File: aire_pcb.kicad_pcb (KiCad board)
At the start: 2 copper layers, 79 x 54.2 mm, 52 parts, among them J1 Conn_01x02_Male, J2 Screw_Terminal_01x02, J3 Screw_Terminal_01x03, J4 Conn_01x04_Male, K1 JRC-21F_4100, K2 JRC-21F_4100, K3 JRC-21F_4100, Q1 2N3904, Q2 2N3904, Q3 2N3904, SW1 SW_Push, SW2 SW_Push, U1 NCP1117-3.3_SOT223, U2 HLK-2M05, U3 SHT40, U4 ESP8266-12E/ESP-12E

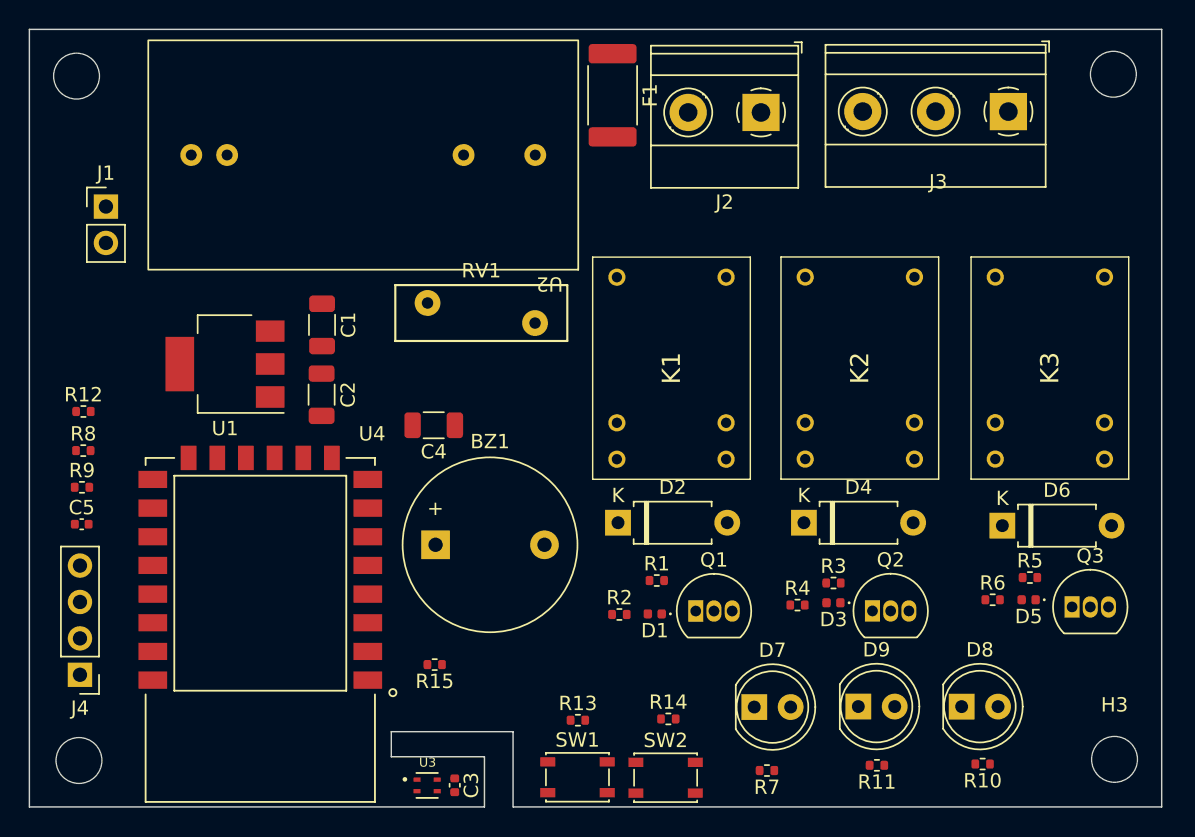
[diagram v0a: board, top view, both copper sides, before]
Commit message: Improve placement and add expansion conenctor
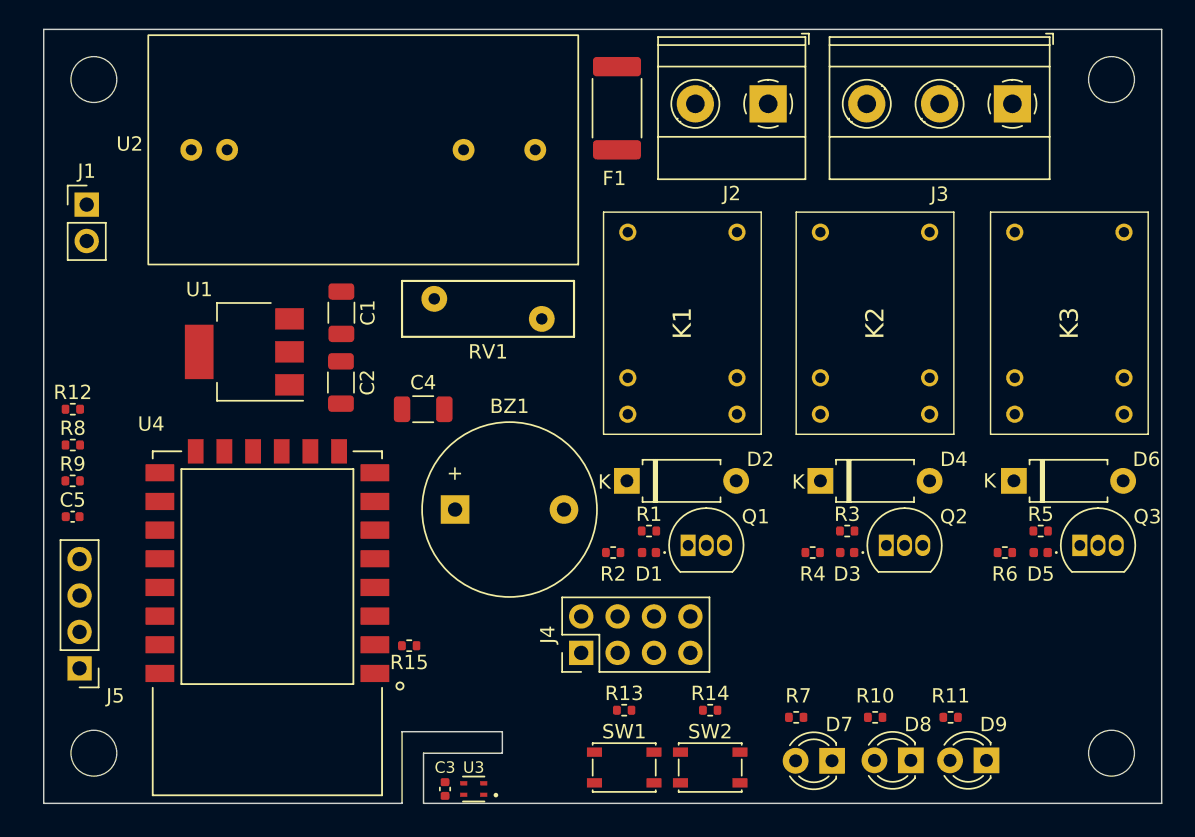
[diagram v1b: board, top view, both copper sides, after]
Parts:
- added J4: Conn_02x04_Top_Bottom, Connector_PinHeader_2.54mm:PinHeader_2x04_P2.54mm_Vertical, F.Cu at (135.0, 107.5)
- D7, D8, D9: footprint LED_THT:LED_D5.0mm -> LED_THT:LED_D3.0mm
- moved D9 9.70 mm to (163.3, 115.0), turned to 180 degrees
- moved R10 8.18 mm to (155.5, 112.0)
- moved D7 6.59 mm to (152.5, 115.0), turned to 180 degrees
- moved R11 6.13 mm to (160.8, 112.0)
- moved D8 5.16 mm to (158.0, 115.0), turned to 180 degrees
- moved Q2 4.68 mm to (156.3, 100.0)
- moved Q1 4.61 mm to (142.5, 100.0)
- moved R2 4.34 mm to (137.2, 100.5)
- moved Q3 4.33 mm to (169.8, 100.0)
- moved D1 4.30 mm to (139.7, 100.5)
- moved R7 4.23 mm to (150.0, 112.0)
- moved R4 3.82 mm to (151.2, 100.5)
- moved R3 3.75 mm to (153.6, 99.0)
- moved D3 3.63 mm to (153.6, 100.5)
- moved R1 3.49 mm to (139.7, 99.0)
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- renumbered J4 to J5
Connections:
- U4 pad 10: unconnected-(U4-Pad10) -> /EXT2
- U4 pad 13: unconnected-(U4-Pad13) -> /EXT1
- U4 pad 2: unconnected-(U4-Pad2) -> /ADC
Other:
- board size 79 x 54.2 mm -> 78 x 54 mm

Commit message: Add serigraphy
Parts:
- moved J4 7.52 mm to (142.5, 107.0)
- moved SW2 4.25 mm to (148.2, 115.5)
- moved R13 3.48 mm to (136.8, 114.8), turned to 90 degrees
- moved R14 3.34 mm to (144.8, 114.8), turned to 90 degrees
- moved D7 3.00 mm to (155.5, 115.0)
- moved D8 3.00 mm to (161.0, 115.0)
- moved D9 3.00 mm to (166.3, 115.0)
- moved R10 3.00 mm to (158.5, 112.0)
- moved R11 3.00 mm to (163.8, 112.0)
- moved R7 3.00 mm to (153.0, 112.0)
- moved J1 2.51 mm to (101.5, 78.5), turned to 180 degrees
- moved SW1 2.25 mm to (140.2, 115.5)
- moved R15 2.06 mm to (123.5, 105.0)
- moved C3 1.00 mm to (126.5, 117.0)
- moved U3 1.00 mm to (128.5, 117.0)
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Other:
- outline, holes or cut-outs redrawn
- board text added: "3V3"
- board text added: "5V"
- board text added: "ADC"
- board text added: "Aire PCB v1.0"
- board text added: "EX1"
- board text added: "EX2"
- board text added: "FLASH"
- board text added: "GND"
- board text added: "Guillermo González"
- board text added: "RESET"
- board text added: "SCL"
- board text added: "SDA"
- board text added: "Septiembre 2022"

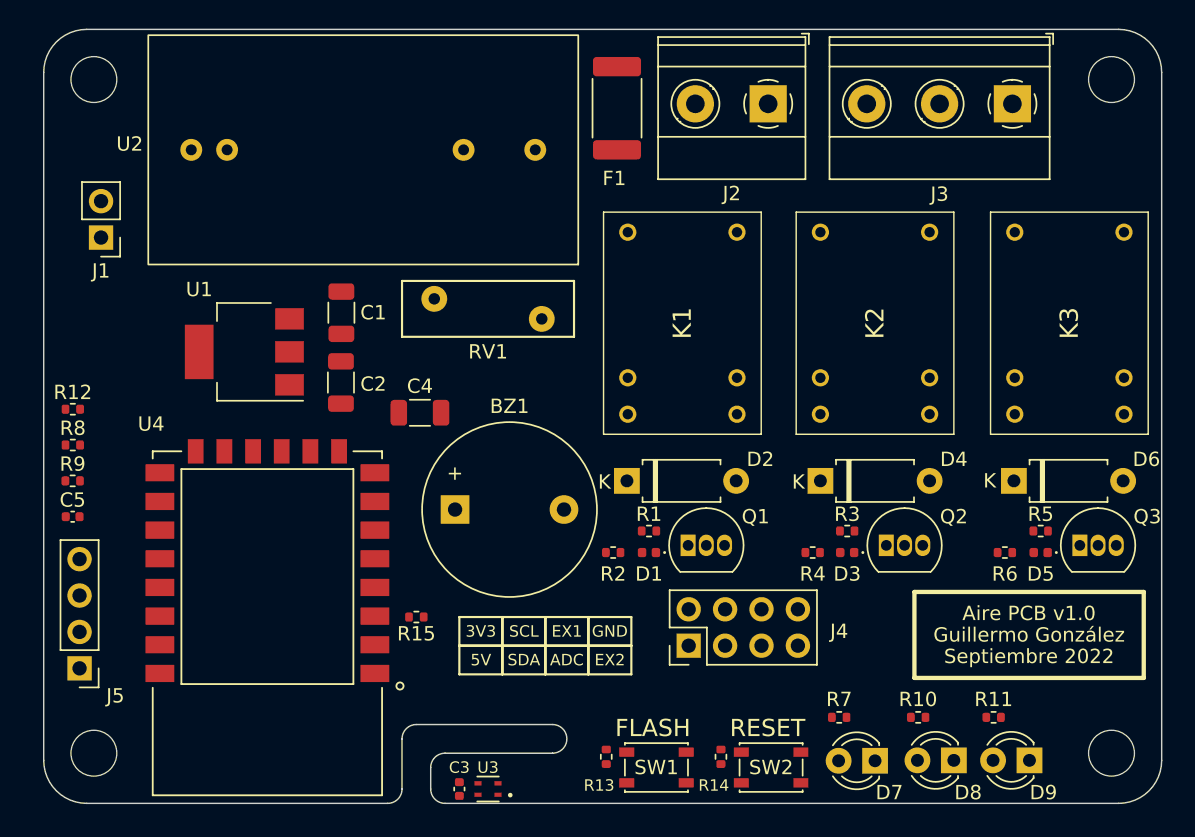
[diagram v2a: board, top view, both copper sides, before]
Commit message: Route PCB with DRC ok
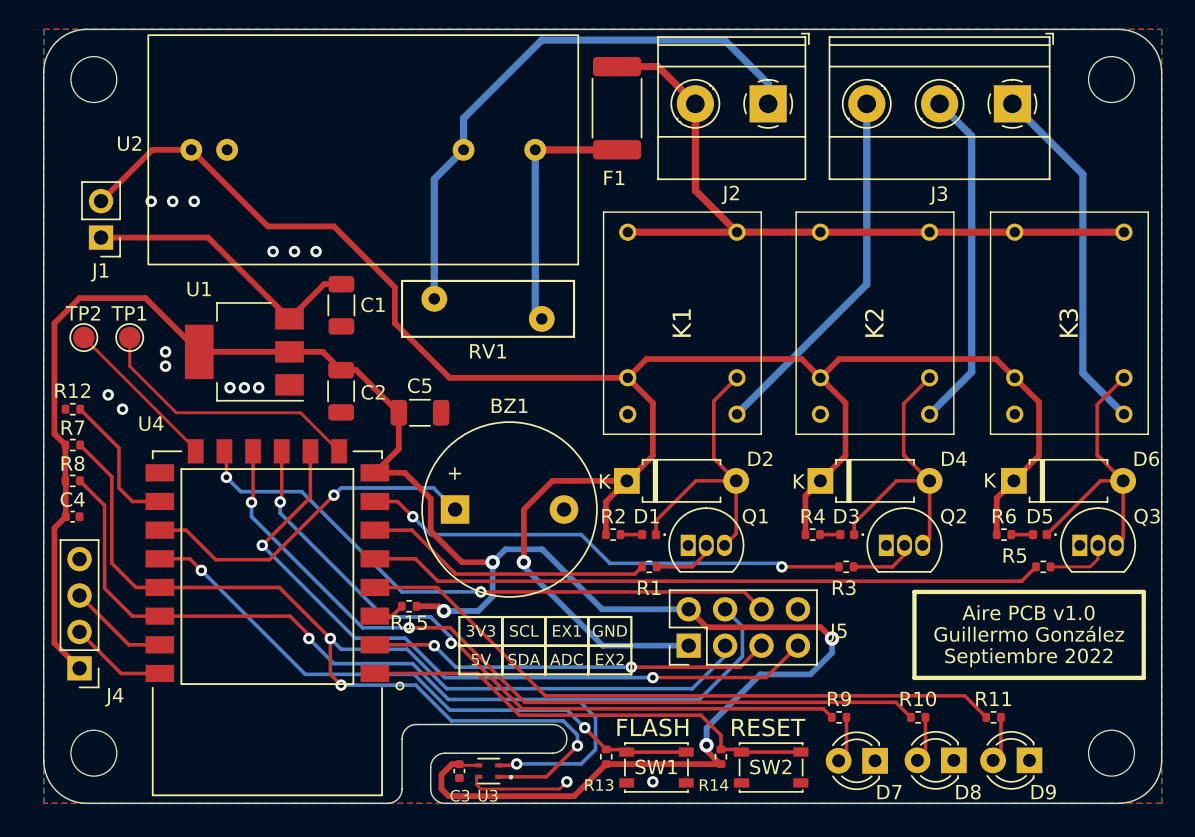
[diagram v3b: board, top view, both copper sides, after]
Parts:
- added TP1: TestPoint, TestPoint:TestPoint_Pad_D1.5mm, F.Cu at (103.5, 85.5)
- added TP2: TestPoint, TestPoint:TestPoint_Pad_D1.5mm, F.Cu at (100.3, 85.5)
- moved R5 2.51 mm to (167.2, 101.5)
- moved R3 2.50 mm to (153.5, 101.5)
- moved R1 2.50 mm to (139.8, 101.5)
- moved D5 1.25 mm to (167.0, 99.2)
- moved R6 1.25 mm to (164.5, 99.2), turned to 180 degrees
- moved U3 1.25 mm to (128.6, 115.8)
- moved D1 1.25 mm to (139.7, 99.2)
- moved R2 1.25 mm to (137.2, 99.2), turned to 180 degrees
- moved C3 1.25 mm to (126.5, 115.8)
- moved D3 1.25 mm to (153.6, 99.2)
- moved R4 1.25 mm to (151.2, 99.2), turned to 180 degrees
- moved R15 0.90 mm to (123.0, 104.2)
- moved C2 0.61 mm to (118.2, 89.2)
- moved C1 0.52 mm to (118.3, 83.2)
- turned R12 to 180 degrees
- renumbered C5 to C4, C4 to C5, J5 to J4, J4 to J5, R8 to R7, R9 to R8, R7 to R9
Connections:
- C1 pad 1: +5V -> Net-(U1-Pad3)
- J1 pad 1: Net-(J1-Pad1) -> Net-(U1-Pad3)
- U1 pad 3: Net-(J1-Pad1) -> Net-(U1-Pad3)
- U4 pad 14: unconnected-(U4-Pad14) -> Net-(TP2-Pad1)
- U4 pad 9: unconnected-(U4-Pad9) -> Net-(TP1-Pad1)
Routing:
- net +3V3: track 0.00 -> 144.9 mm, vias 0 -> 4
- net +5V: track 0.00 -> 140.0 mm, vias 0 -> 1
- net /SDA: track 0.00 -> 85.9 mm, vias 0 -> 3
- net /SCL: track 0.00 -> 72.3 mm, vias 0 -> 2
- net /LED2: track 0.00 -> 56.4 mm, vias 0 -> 2
- net /L: track 0.00 -> 51.3 mm
- net /EXT2: track 0.00 -> 50.1 mm, vias 0 -> 2
- net /LED1: track 0.00 -> 49.0 mm, vias 0 -> 2
- net /FAN3: track 0.00 -> 47.2 mm
- net /LED3: track 0.00 -> 46.4 mm
- net /EXT1: track 0.00 -> 43.0 mm, vias 0 -> 2
- net /GPIO0: track 0.00 -> 42.3 mm, vias 0 -> 2
- net /N: track 0.00 -> 39.6 mm
- net /FAN2: track 0.00 -> 34.3 mm, vias 0 -> 2
- net /nRST: track 0.00 -> 32.6 mm
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- added copper zone on B.Cu, net GND
- added copper zone on F.Cu, net GND

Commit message: Change transistors and diodes to SMD
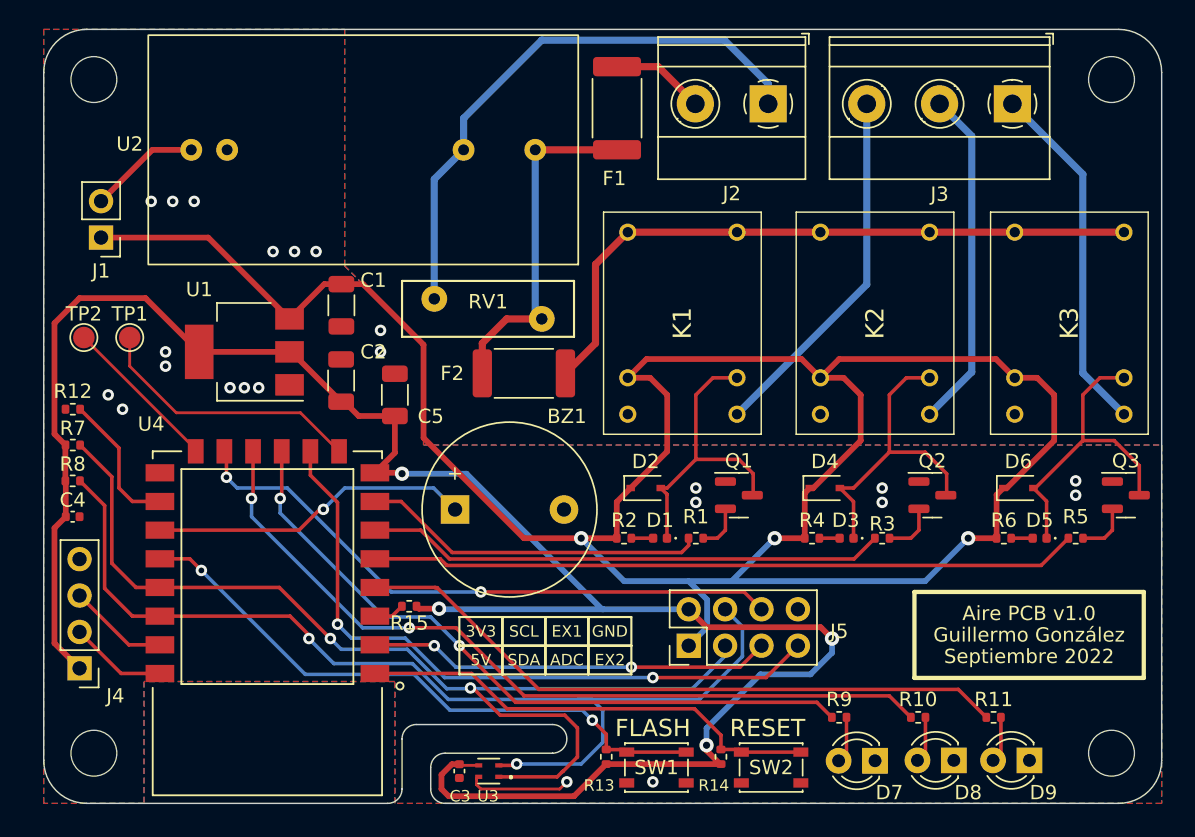
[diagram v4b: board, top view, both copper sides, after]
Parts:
- added F2: Fuse, guille_3rdparty:Fuse_2512_6332Metric, F.Cu at (131.0, 88.0)
- D2, D4, D6: footprint Diode_THT:D_A-405_P7.62mm_Horizontal -> Diode_SMD:D_SOD-323
- Q1, Q2, Q3: footprint Package_TO_SOT_THT:TO-92_Inline -> Package_TO_SOT_SMD:SOT-23
- moved Q1 4.98 mm to (146.0, 96.5)
- moved Q2 4.75 mm to (159.5, 96.5)
- moved Q3 4.75 mm to (173.0, 96.5)
- moved R1 3.82 mm to (143.0, 99.5)
- moved R3 3.21 mm to (156.0, 99.5)
- moved R5 3.02 mm to (169.5, 99.5)
- moved C5 2.15 mm to (122.0, 89.5), turned to 90 degrees
- moved D2 1.40 mm to (139.5, 96.0)
- moved D1 0.80 mm to (140.5, 99.5)
- moved R2 0.80 mm to (138.0, 99.5)
- moved C2 0.75 mm to (118.2, 88.5), turned to 90 degrees
- moved D4 0.59 mm to (152.0, 96.0)
- moved D6 0.59 mm to (165.5, 96.0)
- moved D3 0.25 mm to (153.5, 99.5)
- moved R4 0.25 mm to (151.1, 99.5)
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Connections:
- C1 pad 1: Net-(U1-Pad3) -> +5V
- J1 pad 1: Net-(U1-Pad3) -> +5V
- J1 pad 2: +5V -> Net-(J1-Pad2)
- K1 pad 1: /L -> /LF
- K1 pad 6: /L -> /LF
- K2 pad 1: /L -> /LF
- K2 pad 6: /L -> /LF
- K3 pad 1: /L -> /LF
- K3 pad 6: /L -> /LF
- U1 pad 3: Net-(U1-Pad3) -> +5V
- U2 pad 4: +5V -> Net-(J1-Pad2)
- U4 pad 6: /FAN1 -> /FAN2
- U4 pad 7: /FAN2 -> /FAN1
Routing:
- net /LF: track 0.00 -> 46.3 mm
- net /L: track 51.3 -> 6.54 mm
- net +5V: track 140.0 -> 167.8 mm, vias 1 -> 3
- net Net-(U1-Pad3): track 20.1 -> 0.00 mm
- net /SDA: track 85.9 -> 73.9 mm, vias 3 -> 2
- net Net-(J1-Pad2): track 0.00 -> 7.78 mm
- net Net-(F1-Pad2): track 17.7 -> 24.6 mm
- net /FAN1: track 20.1 -> 24.1 mm
- net /EXT2: track 50.1 -> 47.4 mm
- net +3V3: track 144.9 -> 147.1 mm
- net /FAN3: track 47.2 -> 49.4 mm
- net /FAN2: track 34.3 -> 36.3 mm, vias 2 -> 0
- net /BUZZ: track 24.1 -> 22.4 mm
- net Net-(D5-Pad1): track 20.3 -> 22.0 mm
- net Net-(Q1-Pad2): track 4.40 -> 3.27 mm
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
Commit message: Change mains tracks width and improve serigraphy
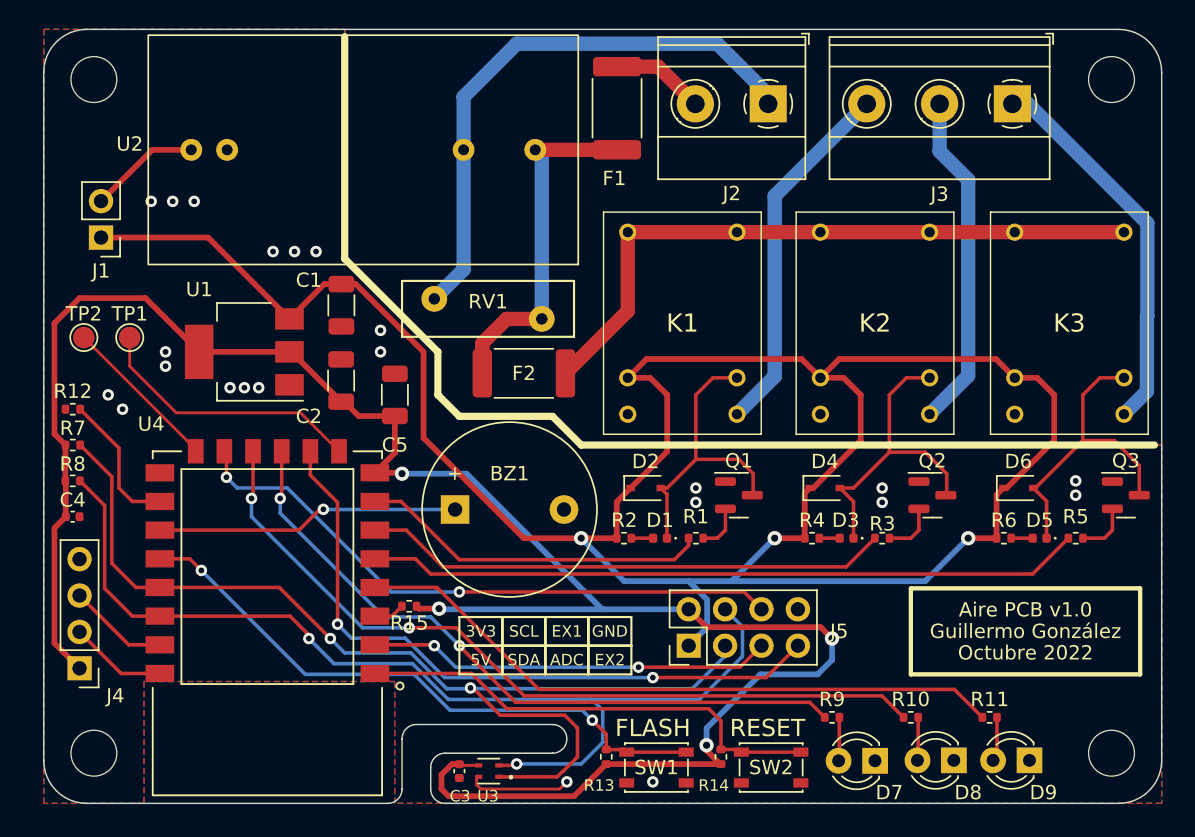
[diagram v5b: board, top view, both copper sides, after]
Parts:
- moved R10 0.51 mm to (158.0, 112.0)
- moved R9 0.50 mm to (152.5, 112.0)
- moved R11 0.28 mm to (163.5, 112.0)
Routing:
- net /P3: track 24.9 -> 26.9 mm
- net /BUZZ: track 22.4 -> 21.2 mm
- net /nRST: track 32.6 -> 33.2 mm
- net /LED2: track 56.4 -> 55.9 mm
- net /LED1: track 48.8 -> 48.3 mm
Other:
- board text added: "Octubre 2022"
- board text removed: "Septiembre 2022"

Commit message: Minor redesign
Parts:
- removed F2: Fuse, guille_3rdparty:Fuse_2512_6332Metric
- removed J4: Conn_01x04_Male, Connector_PinHeader_2.54mm:PinHeader_1x04_P2.54mm_Vertical
- removed U1: NCP1117-3.3_SOT223, Package_TO_SOT_SMD:SOT-223-3_TabPin2
- added C6: 100n, Capacitor_SMD:C_0402_1005Metric, F.Cu at (168.0, 110.0)
- added J6: Conn_01x03_Socket, Connector_PinSocket_2.54mm:PinSocket_1x03_P2.54mm_Vertical, F.Cu at (171.5, 103.0)
- added J7: Conn_01x02_Pin, Connector_PinHeader_2.54mm:PinHeader_1x02_P2.54mm_Vertical, F.Cu at (101.5, 78.8)
- added U5: NCP1117-3.3_SOT223, Package_TO_SOT_SMD:SOT-223-3_TabPin2, F.Cu at (111.0, 86.5)
- H1, H2, H3, H4: footprint MountingHole:MountingHole_3.2mm_M3_DIN965 -> MountingHole:MountingHole_3.2mm_M3_Pad_TopBottom
- J1: value Conn_01x02_Male -> Conn_01x04_Pin; footprint Connector_PinHeader_2.54mm:PinHeader_1x02_P2.54mm_Vertical -> Connector_PinHeader_2.54mm:PinHeader_1x04_P2.54mm_Vertical
- moved J1 30.1 mm to (100.0, 108.6)
- moved BZ1 10.6 mm to (124.7, 87.0)
- moved RV1 5.70 mm to (132.2, 78.5)
- moved J2 1.80 mm to (149.8, 69.2)
- moved C5 1.50 mm to (120.5, 89.5)
- moved C1 0.75 mm to (117.5, 83.2)
- moved C2 0.75 mm to (117.5, 88.5)
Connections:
- net /EXT2 renamed /TEMP
- F1 pad 2: Net-(F1-Pad2) -> /LF
- J1 pad 1: +5V -> +3V3
- J1 pad 2: Net-(J1-Pad2) -> /TX
- RV1 pad 1: Net-(F1-Pad2) -> /LF
- U2 pad 1: Net-(F1-Pad2) -> /LF
- U2 pad 4: Net-(J1-Pad2) -> Net-(J7-Pin_2)
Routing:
- net Net-(F1-Pad2): track 24.6 -> 0.00 mm
- net /TEMP: track 47.4 -> 70.1 mm
- net Net-(J7-Pin_2): track 0.00 -> 7.88 mm
- net Net-(J1-Pad2): track 7.78 -> 0.00 mm
- net /LF: track 46.3 -> 52.7 mm
- net +5V: track 167.5 -> 173.0 mm
- net /BUZZ: track 21.2 -> 25.8 mm
- net /N: track 39.8 -> 35.6 mm
- net /L: track 6.54 -> 7.79 mm
- net +3V3: track 147.4 -> 146.5 mm
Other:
- board text added: "Abril 2023"
- board text added: "Power switch"
- board text added: "RX"
- board text added: "TMP"
- board text added: "TX"
- board text removed: "Octubre 2022"

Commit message: PCB changes
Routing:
- net +5V: track 173.0 -> 186.7 mm
- net GND: vias 23 -> 49
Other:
- board text added: "L"
- board text added: "N"
- board text added: "P1"
- board text added: "P2"
- board text added: "P3"
